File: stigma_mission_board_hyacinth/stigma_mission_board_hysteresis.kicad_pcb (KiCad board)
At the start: 4 copper layers, 50 x 150 mm, 207 parts, among them J1 DF40C-70DS-0.4V(51), J2 DF40HB(2.5)-10DS-0.4V(51), J7 SMA, J8 SMA, J9 JST-GH 4Pin, Q1 DMN2056U, Q2 DMN2056U, Q3 AOSP21321, Q4 DMN2056U, Q5 AOSP21321, Q6 DMN2056U, Q7 AOSP21321, Q8 DMN2056U, Q9 AOSP21321, U1 LAN8742A, U10 MCP2562-E-SN, U11 MCP2562-E-SN, U12 SN74HCS594, U13 INA181, U14 INA181, U15 INA181, U16 INA181, U2 INA181, U3 TPD4E1U06, U4 L7805, U5 L7805, U6 AZ1117H-ADJ, U7 AZ1117H-ADJ, U8 Ai-Thinker-Ra-01, U9 Ai-Thinker-Ra-01, Y1 25MHz

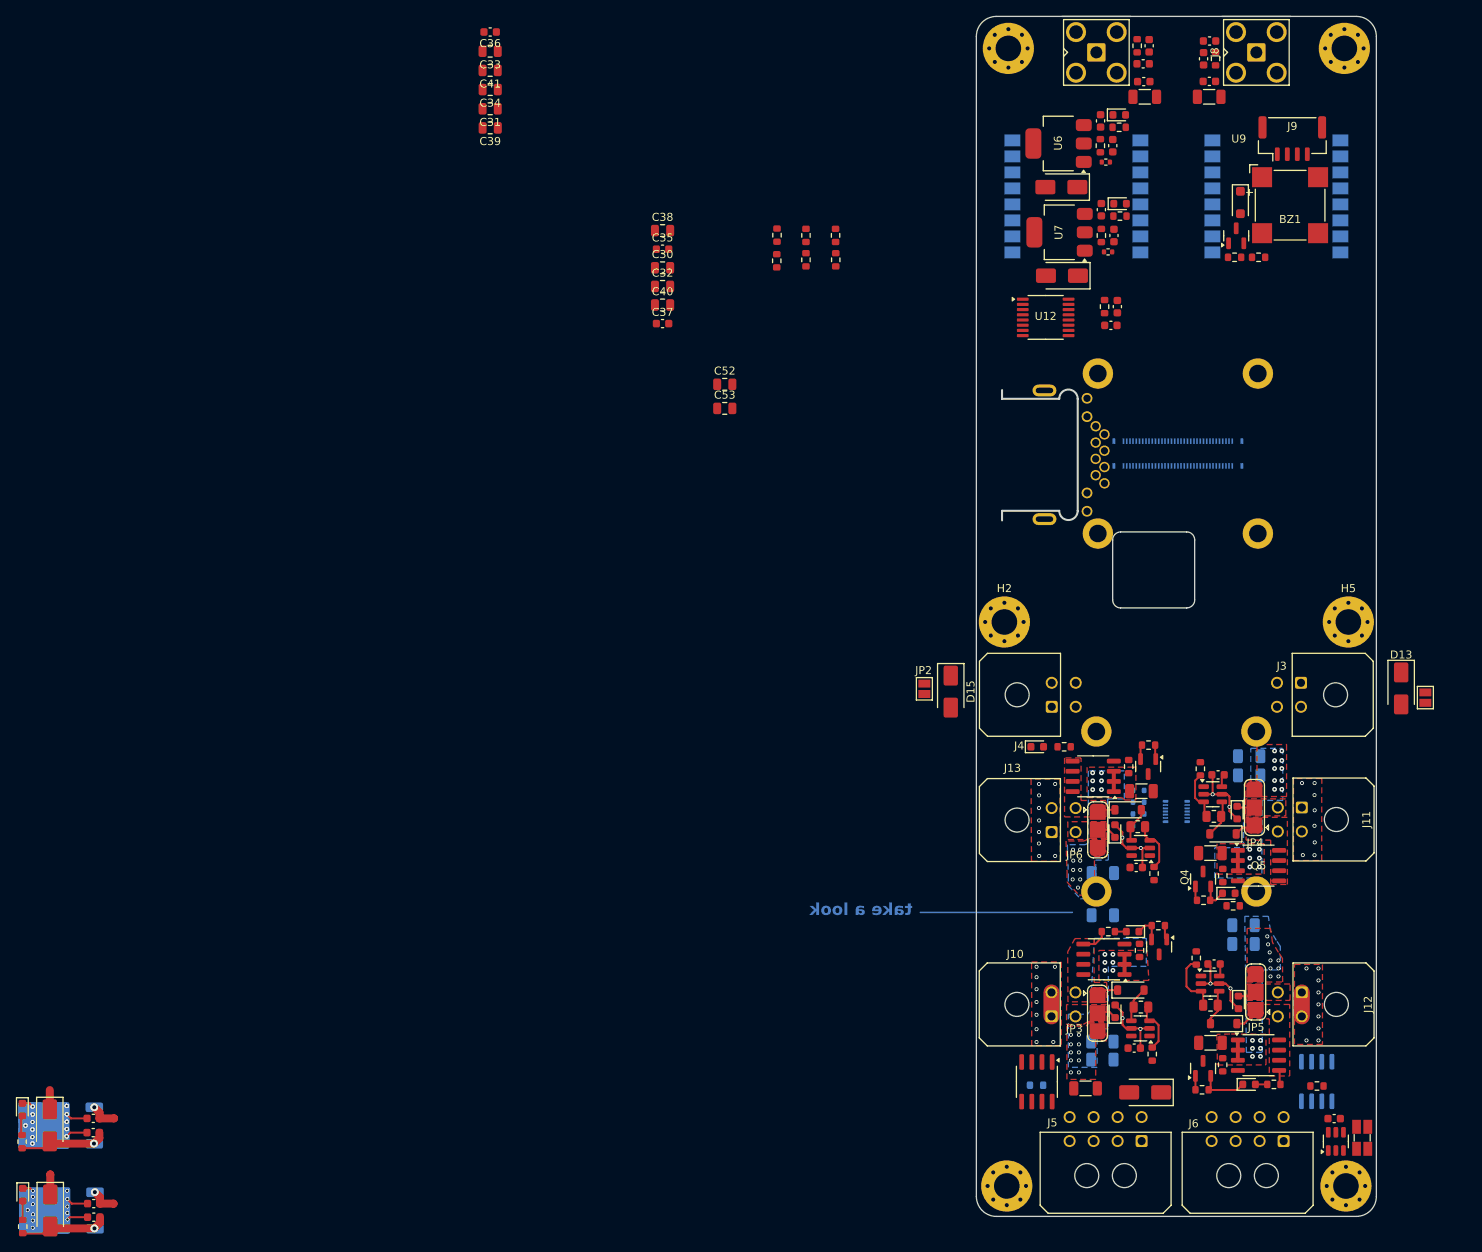
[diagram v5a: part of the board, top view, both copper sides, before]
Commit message: added 5v regulators to pcb
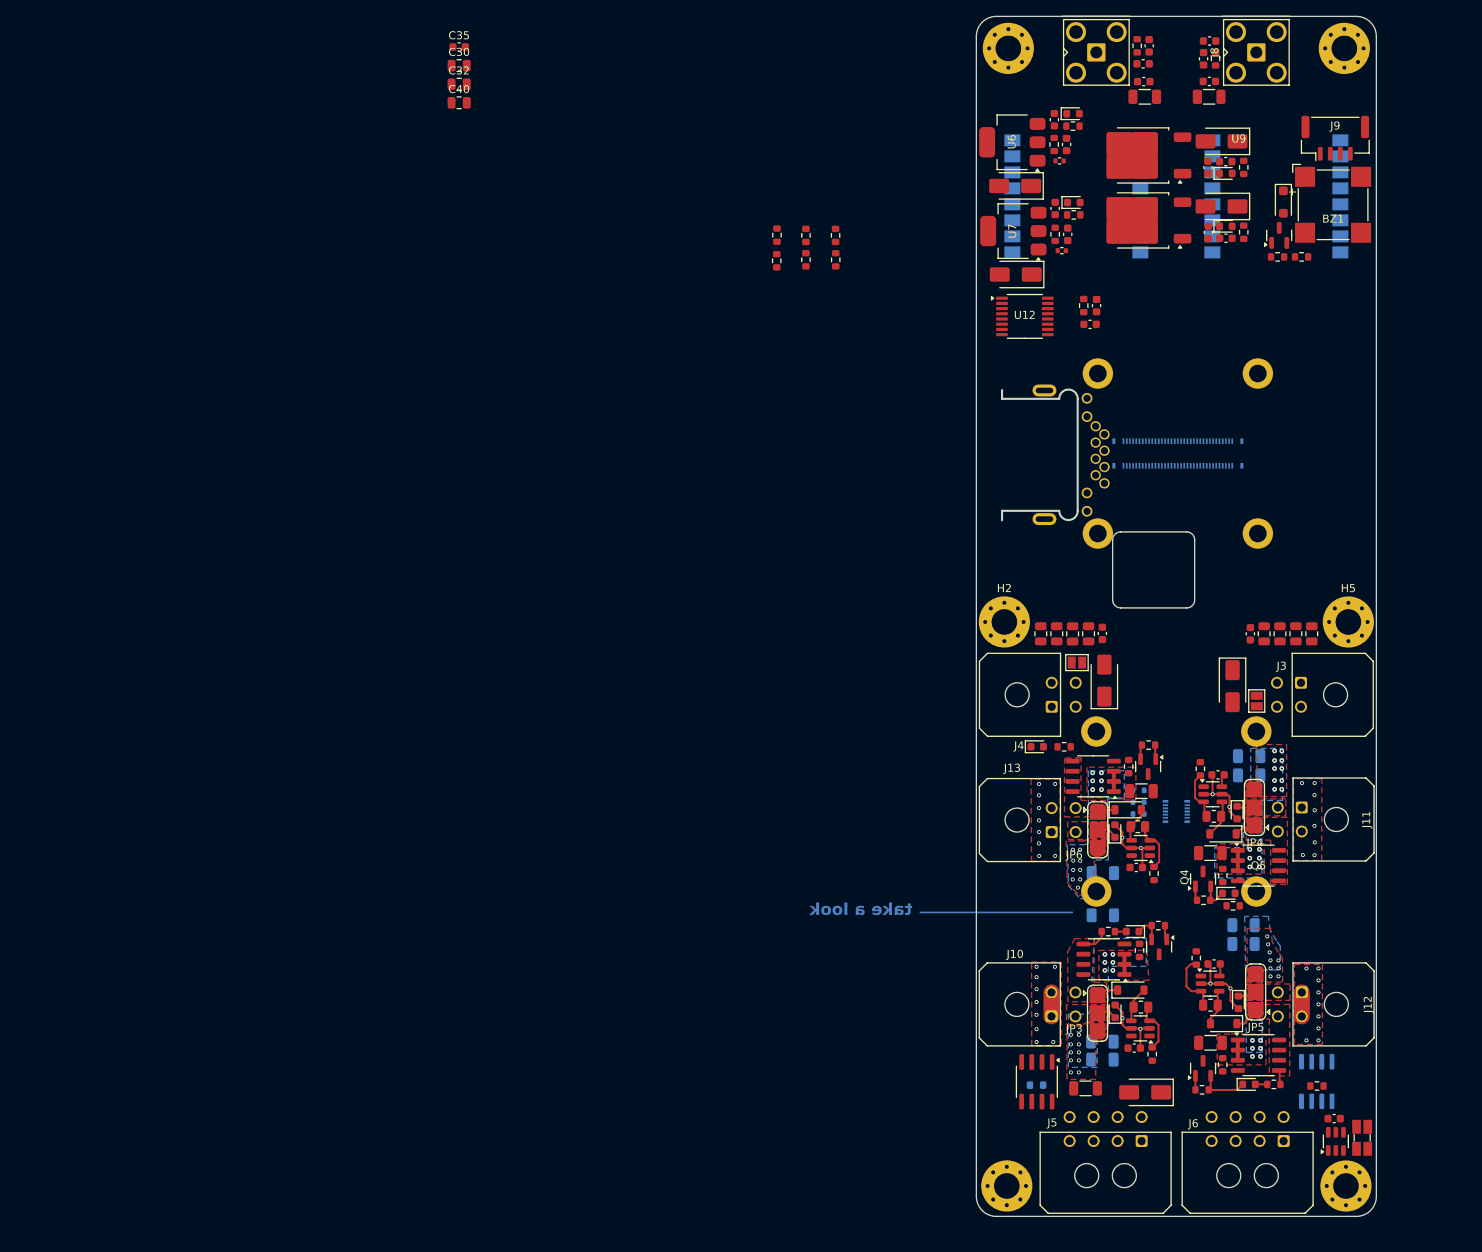
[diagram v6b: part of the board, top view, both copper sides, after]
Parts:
- U4, U5: moved to F.Cu
- moved R35 196.8 mm to (233.4, 127.0)
- moved R34 195.3 mm to (233.4, 118.9), turned to -90 degrees
- moved D8 193.1 mm to (231.2, 126.2), turned to 0 degrees
- moved D6 192.8 mm to (230.7, 123.8), turned to 180 degrees
- moved D5 191.3 mm to (230.7, 115.6), turned to 180 degrees
- moved D7 190.6 mm to (231.2, 119.6), turned to 0 degrees
- moved C19 187.1 mm to (231.2, 127.7)
- moved C18 186.5 mm to (231.2, 118.2)
- moved C17 184.8 mm to (229.0, 127.0), turned to -90 degrees
- moved U5 183.8 mm to (220.7, 125.5)
- moved C16 183.1 mm to (228.9, 118.9), turned to -90 degrees
- moved U4 182.2 mm to (220.7, 117.4)
- moved C41 124.5 mm to (241.9, 177.2), turned to -90 degrees
- moved C39 117.2 mm to (237.9, 177.2), turned to -90 degrees
- moved C36 107.3 mm to (215.8, 177.1), turned to -90 degrees
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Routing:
- net GND: track 74.4 -> 58.5 mm, vias 67 -> 43
- net Net-(D6-A): track 11.1 -> 0.00 mm, vias 1 -> 0
- net Net-(D5-A): track 11.1 -> 0.00 mm, vias 1 -> 0
- net main_voltage: track 6.91 -> 0.00 mm, vias 2 -> 0
- net +5V: track 4.92 -> 0.00 mm
- net Net-(D7-A): track 2.49 -> 0.00 mm
- net Net-(D8-A): track 2.40 -> 0.00 mm

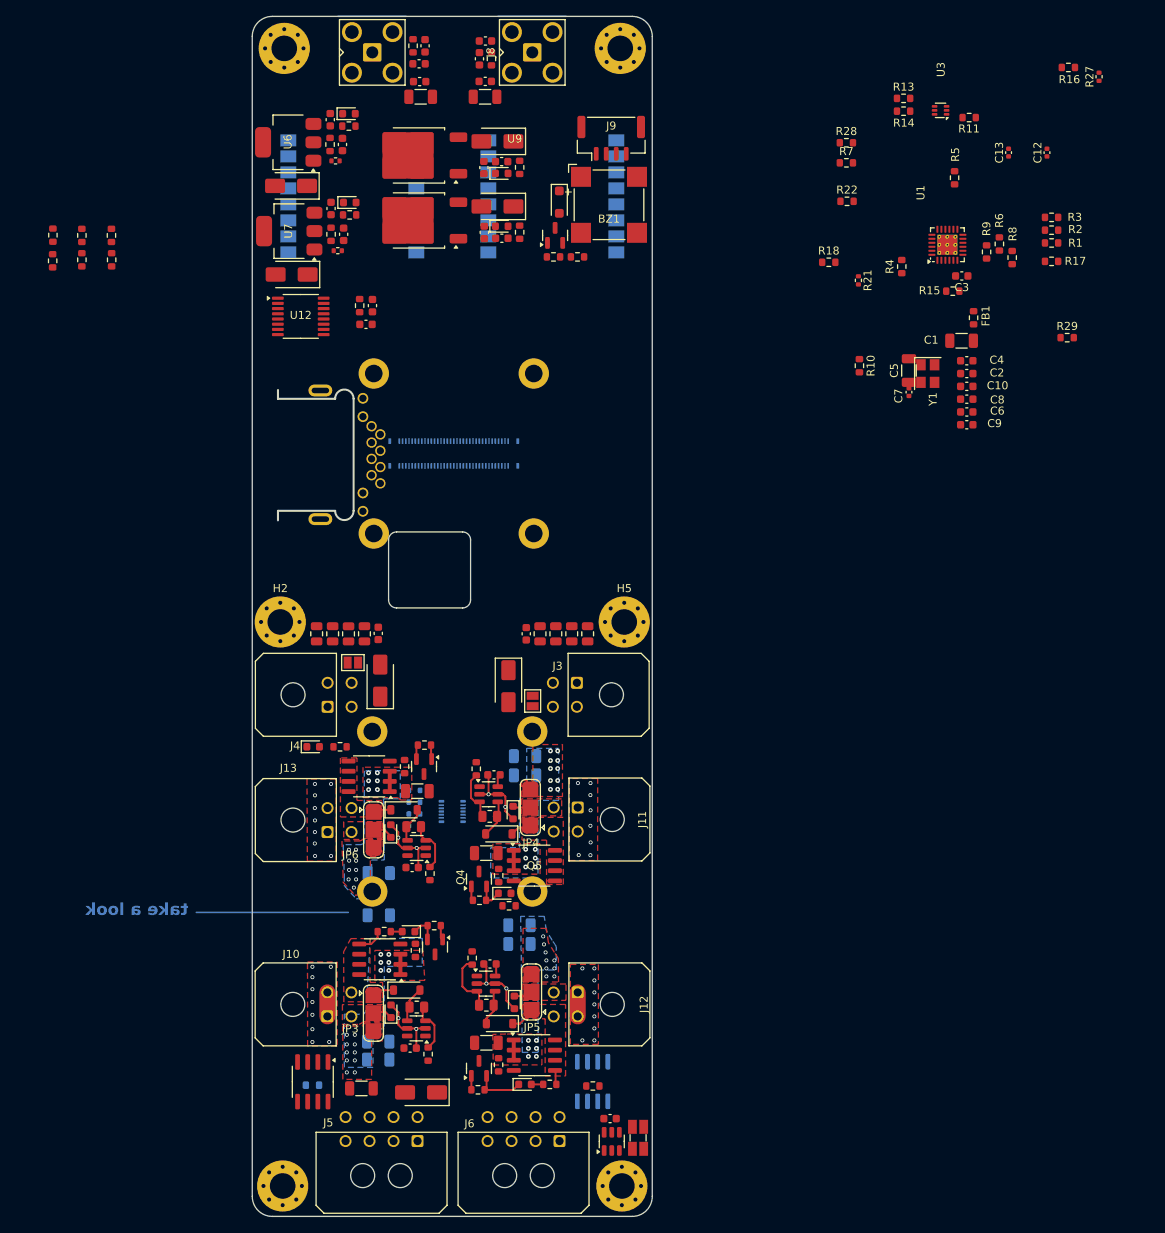
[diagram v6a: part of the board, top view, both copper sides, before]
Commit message: added ethernet layout to pcb and changed minor errors
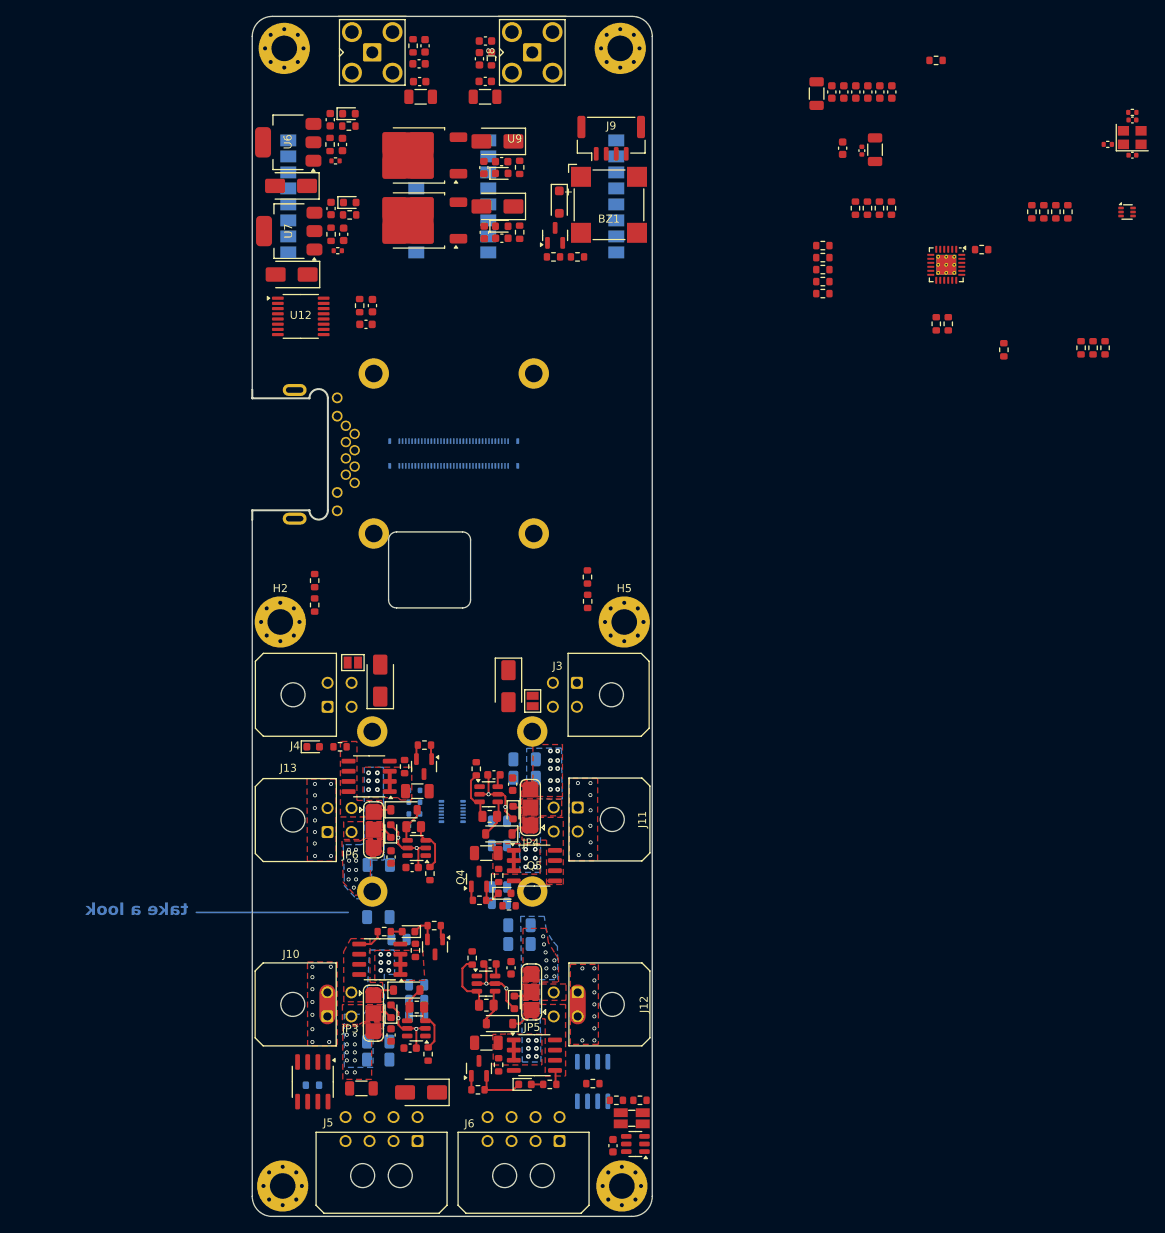
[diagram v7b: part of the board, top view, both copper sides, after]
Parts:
- added C54: 1u, Capacitor_SMD:C_0603_1608Metric, F.Cu at (232.3, 218.9)
- added C55: 1u, Capacitor_SMD:C_0603_1608Metric, F.Cu at (217.3, 205.1)
- C31, C33, C34, C38, C39, C41, C52, C53: moved to B.Cu
- moved R20 129.1 mm to (245.5, 235.5), turned to 180 degrees
- moved R19 128.1 mm to (248.5, 235.5), turned to 180 degrees
- moved R23 73.2 mm to (241.9, 173.1)
- moved R24 73.2 mm to (241.9, 170.1)
- moved R26 52.0 mm to (207.8, 170.5)
- moved R25 52.0 mm to (207.8, 173.6)
- moved C36 50.2 mm to (217.3, 227.3)
- moved C33 49.5 mm to (220.6, 225.0), turned to 180 degrees
- moved C34 47.0 mm to (220.6, 223.0), turned to 180 degrees
- moved C31 44.7 mm to (220.6, 221.1), turned to 180 degrees
- moved C9 42.6 mm to (279.9, 109.4), turned to -90 degrees
- moved C6 41.4 mm to (278.4, 109.4), turned to -90 degrees
- moved C8 40.3 mm to (276.9, 109.4), turned to -90 degrees
- moved R28 40.1 mm to (305.1, 141.4), turned to -90 degrees
- moved C10 39.3 mm to (275.4, 109.4), turned to -90 degrees
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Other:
- outline, holes or cut-outs redrawn
- board text removed: "Voltage & Current Sensing"

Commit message: Temp save of changes. Changed PCB size, layout and number of Connectors
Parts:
- moved C15 177.0 mm to (386.9, 122.4)
- moved C22 177.0 mm to (398.6, 102.1)
- moved C24 177.0 mm to (397.9, 104.3)
- moved C27 177.0 mm to (406.1, 108.5)
- moved C36 177.0 mm to (394.4, 225.7)
- moved C45 177.0 mm to (396.7, 227.4)
- moved C52 177.0 mm to (395.3, 213.8)
- moved C54 177.0 mm to (409.4, 217.3)
- moved C55 177.0 mm to (394.4, 203.5)
- moved D14 177.0 mm to (398.1, 232.9)
- moved D18 177.0 mm to (396.5, 212.8)
- moved D19 177.0 mm to (394.3, 222.8)
- moved D22 177.0 mm to (409.6, 197.9)
- moved D23 177.0 mm to (407.9, 224.3)
- moved D26 177.0 mm to (396.0, 197.6)
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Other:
- outline, holes or cut-outs redrawn
